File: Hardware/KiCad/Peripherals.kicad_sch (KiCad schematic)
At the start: 64 parts, among them Q1 PMBT3904, U1 MPU-6000, U2 HMC5883L, U3 FM24C64B, U4 BMP388

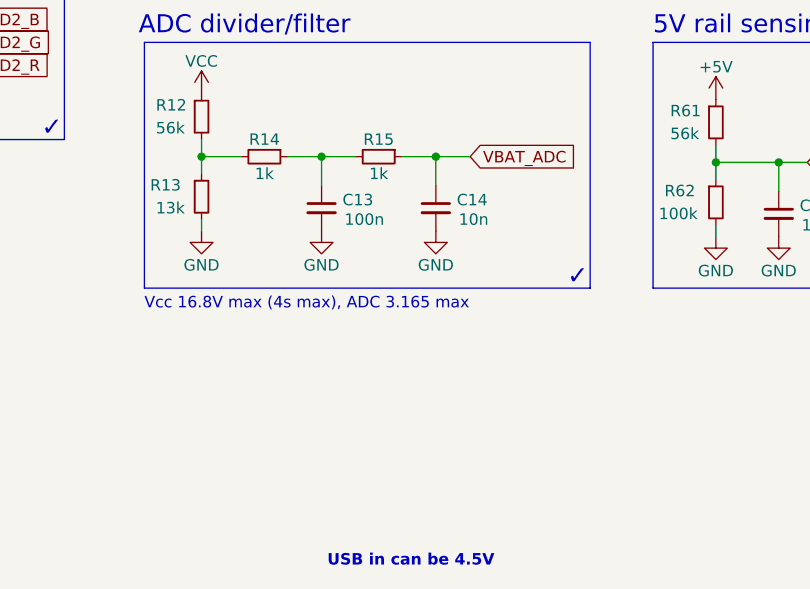
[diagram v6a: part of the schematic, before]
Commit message: Changed the 3.3V LDO to one that supports a lower Vin so sub 5V USB supplies are less likely to pose a problem
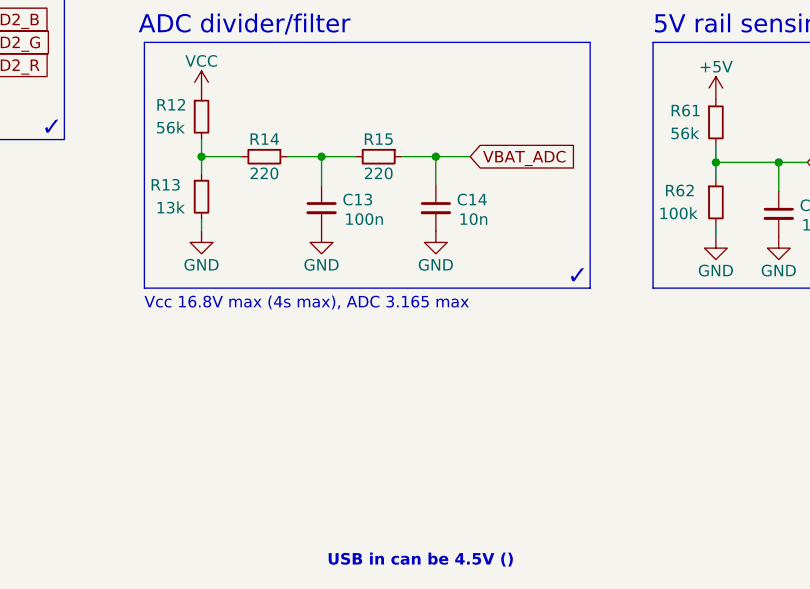
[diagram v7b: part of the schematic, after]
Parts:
- R14, R15: value 1k -> 220
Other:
- note added: "USB in can be 4.5V ()"
- note removed: "USB in can be 4.5V"
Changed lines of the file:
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@@
     (effects (font (size 1.27 1.27)) (justify left bottom))
   )
-  (text "USB in can be 4.5V" (at 117.475 191.135 0)
+  (text "USB in can be 4.5V ()" (at 117.475 191.135 0)
     (effects (font (size 1.27 1.27) (thickness 0.254) bold) (justify left bottom))
   )
@@
     (in_bom yes) (on_board yes)
     (property "Reference" "R14" (id 0) (at 110.49 143.51 90))
-    (property "Value" "1k" (id 1) (at 110.49 147.32 90))
+    (property "Value" "220" (id 1) (at 110.49 147.32 90))
     (property "Footprint" "Resistor_SMD:R_0402_1005Metric" (id 2) (at 110.49 145.415 0)
       (effects (font (size 1.27 1.27)) hide)
@@
     (in_bom yes) (on_board yes)
     (property "Reference" "R15" (id 0) (at 123.19 143.51 90))
-    (property "Value" "1k" (id 1) (at 123.19 147.32 90))
+    (property "Value" "220" (id 1) (at 123.19 147.32 90))
     (property "Footprint" "Resistor_SMD:R_0402_1005Metric" (id 2) (at 123.19 145.415 0)
       (effects (font (size 1.27 1.27)) hide)

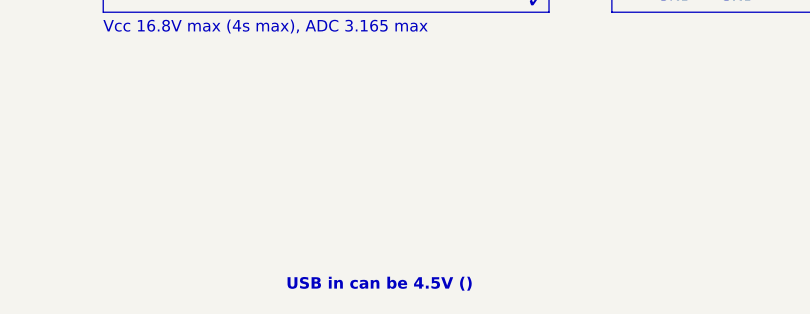
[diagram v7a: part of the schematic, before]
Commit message: SWD was 1mm pitch and needed to be 1.27 mm
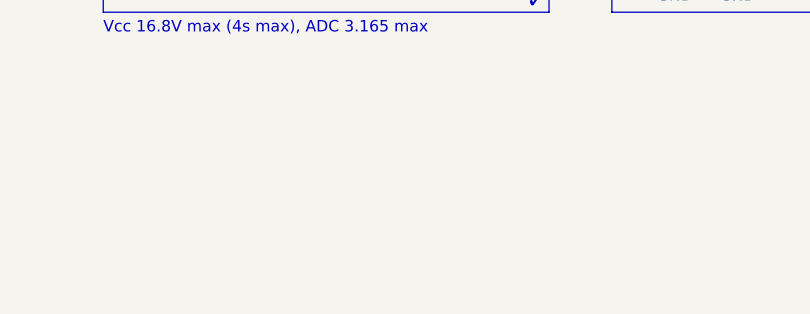
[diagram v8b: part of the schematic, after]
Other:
- note removed: "USB in can be 4.5V ()"
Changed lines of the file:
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@@
     (effects (font (size 1.27 1.27)) (justify left bottom))
-  )
-  (text "USB in can be 4.5V ()" (at 117.475 191.135 0)
-    (effects (font (size 1.27 1.27) (thickness 0.254) bold) (justify left bottom))
   )
   (text "CPOUT = 2.2nF 50V" (at 17.145 82.55 0)
